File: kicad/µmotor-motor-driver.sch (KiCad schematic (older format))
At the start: 7 parts, among them J501 1, J502 2, U501 DRV8870, U502 INA180A1

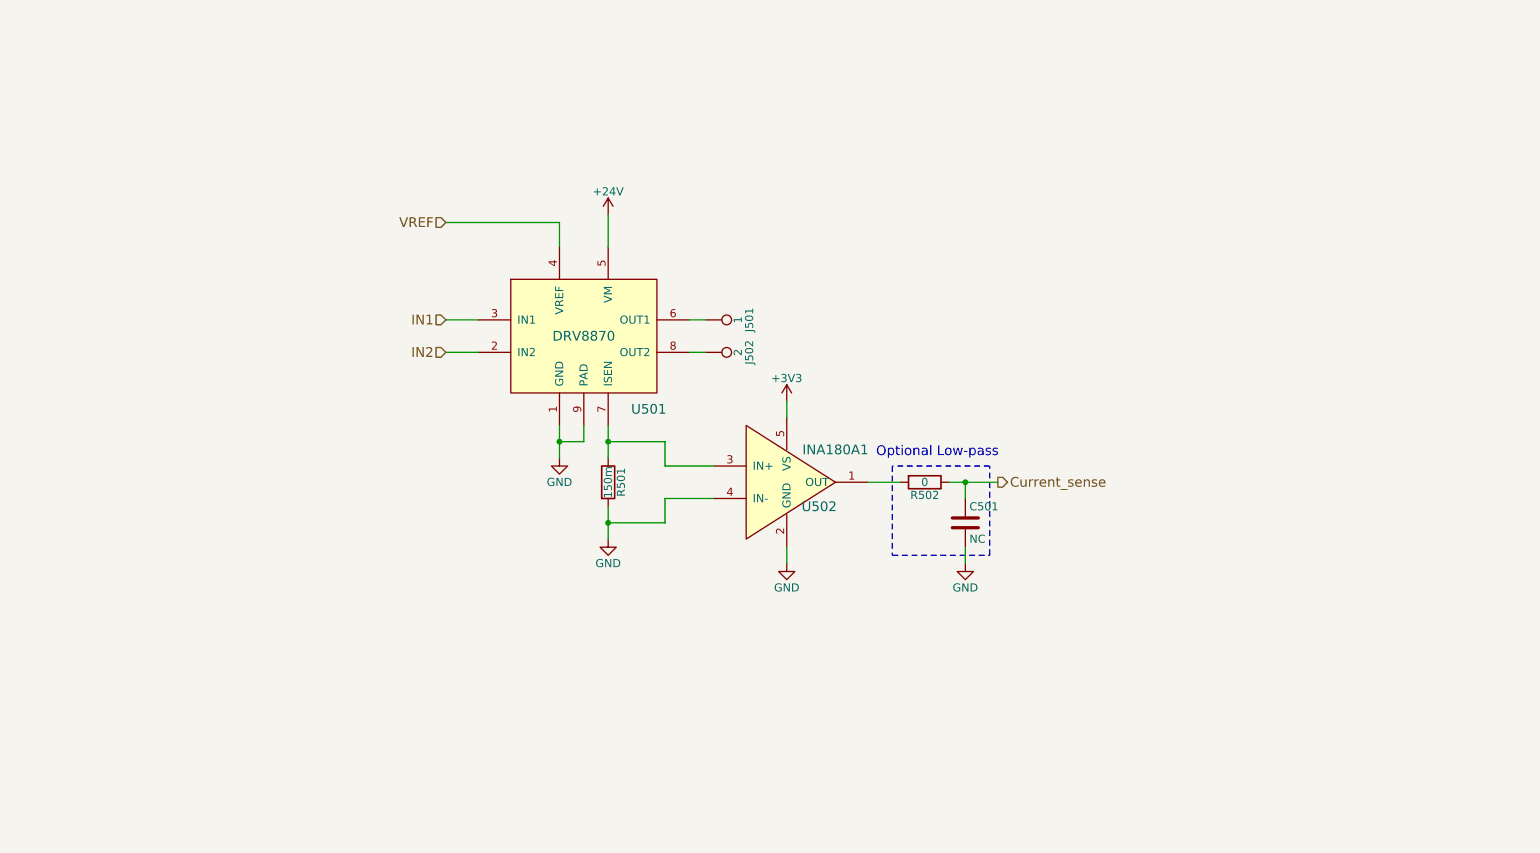
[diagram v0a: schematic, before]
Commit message: second design: STM32L432KC µC with DRV8323S gate driver and FDMD82xx FETs
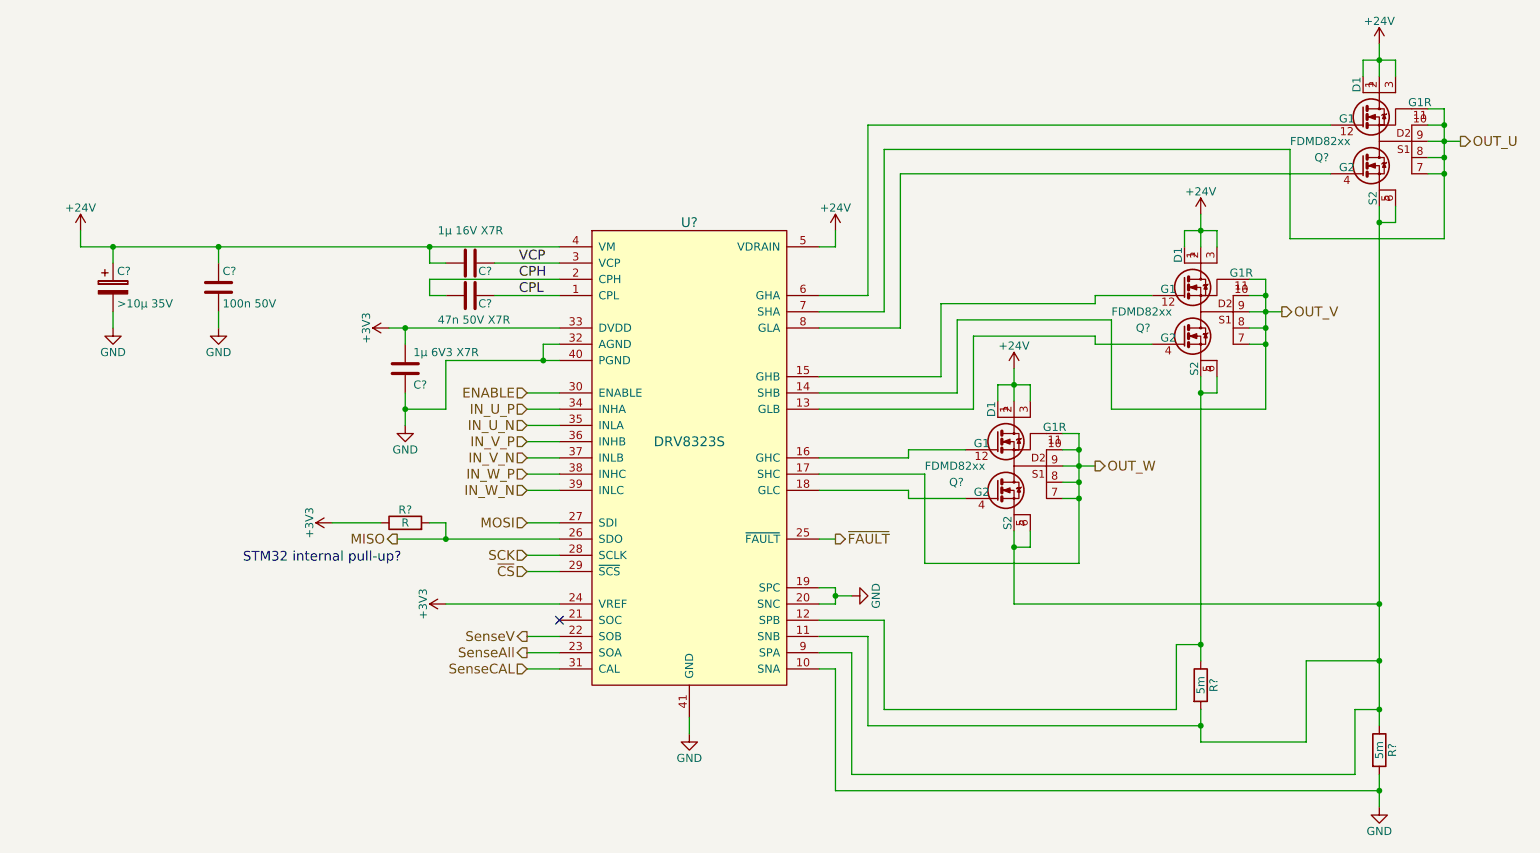
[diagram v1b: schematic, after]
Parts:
- removed C501: NC, Capacitors_SMD:C_0603, symbol C
- removed J501: 1, Measurement_Points:Measurement_Point_Round-SMD-Pad_Small, symbol TEST_1P
- removed J502: 2, Measurement_Points:Measurement_Point_Round-SMD-Pad_Small, symbol TEST_1P
- removed R501: 150m, Resistors_SMD:R_0805, symbol R
- removed R502: 0, Resistors_SMD:R_0603, symbol R
- removed U501: DRV8870, HSOP-8:HSOP-8, symbol DRV8870
- removed U502: INA180A1, TO_SOT_Packages_SMD:SOT-23-5, symbol INA180A
- added C?: 1µ 16V X7R, symbol C
- added C?: 47n 50V X7R, symbol C
- added C?: 100n 50V, symbol C
- added C?: >10µ 35V, symbol CP
- added C?: 1µ 6V3 X7R, symbol C
- added Q? (x3): FDMD82xx, symbol FDMD82xx
- added R?: R, symbol R
- added R? (x2): 5m, symbol R
- added U?: DRV8323S, symbol DRV8323S
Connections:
- net +24V: now also C?.1, C?.1, C?.2, Q?.1 (D1), Q?.1 (D1), Q?.1 (D1), Q?.13 (D1), Q?.13 (D1), Q?.13 (D1), Q?.2, Q?.2, Q?.2, Q?.3, Q?.3, Q?.3, U?.4 (VM), U?.5 (VDRAIN)
- net +3V3: now also C?.1, R?.1, U?.24 (VREF), U?.33 (DVDD)
- net GND: now also C?.2, C?.2, C?.2, R?.2, U?.10 (SNA), U?.19 (SPC), U?.20 (SNC), U?.32 (AGND), U?.40 (PGND), U?.41 (GND)
- new net: Q?.14 (S2), Q?.14 (S2), Q?.5 (S2), Q?.5 (S2), Q?.6, Q?.6, R?.1, R?.2, U?.11 (SNB), U?.9 (SPA)
- new net: Q?.14 (S2), Q?.5 (S2), Q?.6, R?.1, U?.12 (SPB)
- new net: Q?.4 (G2), U?.13 (GLB)
- new net: Q?.12 (G1), U?.15 (GHB)
- new net: Q?.12 (G1), U?.16 (GHC)
- new net: Q?.4 (G2), U?.18 (GLC)
- new net: Q?.12 (G1), U?.6 (GHA)
- new net: Q?.4 (G2), U?.8 (GLA)
- new net CPH: C?.2, U?.2 (CPH)
- new net CPL: C?.1, U?.1 (CPL)
- new net ENABLE: U?.30 (ENABLE)
- new net IN_U_N: U?.35 (INLA)
- new net IN_U_P: U?.34 (INHA)
- new net IN_V_N: U?.37 (INLB)
- new net IN_V_P: U?.36 (INHB)
- new net IN_W_N: U?.39 (INLC)
- new net IN_W_P: U?.38 (INHC)
- new net MISO: R?.2, U?.26 (SDO)
- new net MOSI: U?.27 (SDI)
- new net OUT_U: Q?.10, Q?.11 (G1R), Q?.7, Q?.8, Q?.9, U?.7 (SHA)
- new net OUT_V: Q?.10, Q?.11 (G1R), Q?.7, Q?.8, Q?.9, U?.14 (SHB)
- new net OUT_W: Q?.10, Q?.11 (G1R), Q?.7, Q?.8, Q?.9, U?.17 (SHC)
- new net SCK: U?.28 (SCLK)
- new net SenseAll: U?.23 (SOA)
- new net SenseCAL: U?.31 (CAL)
- new net SenseV: U?.22 (SOB)
- new net VCP: C?.1, U?.3 (VCP)
- new net ~CS: U?.29 (~SCS)
- new net ~FAULT: U?.25 (~FAULT)
- no-connect marks 0 -> 1
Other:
- note added: "STM32 internal pull-up?"
- note removed: "Optional Low-pass"

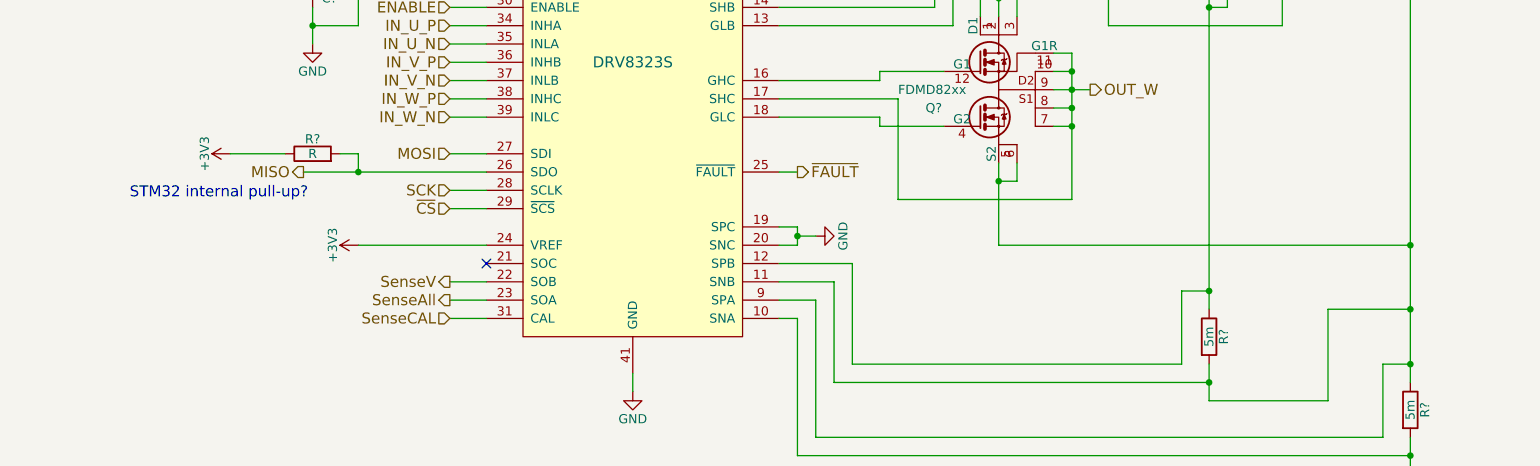
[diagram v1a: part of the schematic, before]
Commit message: update µC pinout, motor driver, CubeMX, add 3V3 regulator and temperature sensor
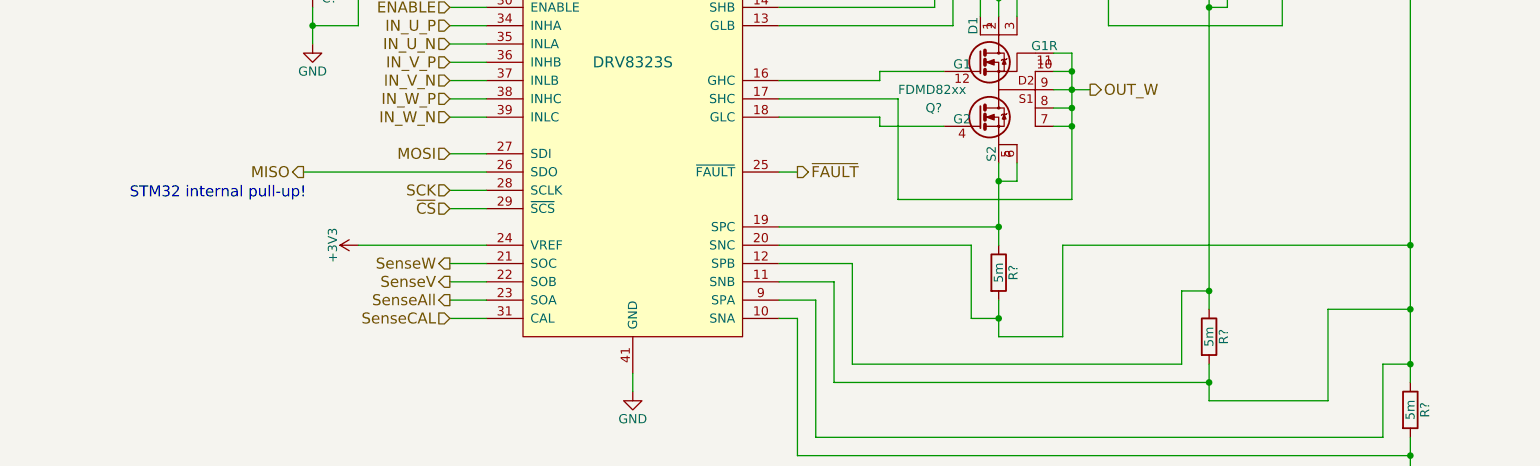
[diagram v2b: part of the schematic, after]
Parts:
- removed R?: R, symbol R
- added R?: 5m, symbol R
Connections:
- net GND: no longer U?.19 (SPC), U?.20 (SNC)
- net at Q?.14 (S2), Q?.5 (S2), Q?.6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: now also U?.20 (SNC), R?.2; no longer Q?.14 (S2), Q?.5 (S2), Q?.6
- net SenseW: now reaches U?.21 (SOC)
- new net: Q?.14 (S2), Q?.5 (S2), Q?.6, R?.1, U?.19 (SPC)
- no-connect marks 1 -> 0
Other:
- note added: "STM32 internal pull-up!"
- note removed: "STM32 internal pull-up?"
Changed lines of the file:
@@
 LIBS:drv8323s
 LIBS:FDMD82xx
+LIBS:ncp4623
+LIBS:TMP006
 LIBS:µmotor-cache
 EELAYER 25 0
@@
 $Descr A4 11693 8268
 encoding utf-8
-Sheet 4 6
+Sheet 3 6
 Title "µmotor - Micro Motor Controller"
 Date "2017-09-14"
@@
 Text HLabel 4850 4900 0    60   Input ~ 0
 ~CS
-$Comp
-L R R?
-U 1 1 5A4FECE8
-P 4100 4600
-F 0 "R?" V 4180 4600 50  0000 C CNN
-F 1 "R" V 4100 4600 50  0000 C CNN
-F 2 "" V 4030 4600 50  0001 C CNN
-F 3 "" H 4100 4600 50  0001 C CNN
-	1    4100 4600
-	0    -1   -1   0
-$EndComp
-$Comp
-L +3V3 #PWR?
-U 1 1 5A4FEE5D
-P 3650 4600
-F 0 "#PWR?" H 3650 4450 50  0001 C CNN
-F 1 "+3V3" H 3650 4740 50  0000 C CNN
-F 2 "" H 3650 4600 50  0001 C CNN
-F 3 "" H 3650 4600 50  0001 C CNN
-	1    3650 4600
-	0    -1   -1   0
-$EndComp
 Text Notes 3100 4850 0    60   ~ 0
-STM32 internal pull-up?
+STM32 internal pull-up!
 $Comp
 L GND #PWR?
@@
 	4850 5500 5050 5500
 Wire Wire Line
-	4250 4600 4350 4600
-Wire Wire Line
-	4350 4600 4350 4700
-Wire Wire Line
 	4050 4700 5050 4700
-Connection ~ 4350 4700
 Wire Wire Line
 	4850 4600 5050 4600
@@
 Wire Wire Line
 	4850 4900 5050 4900
-Wire Wire Line
-	3650 4600 3950 4600
 Wire Wire Line
 	5850 5900 5850 5800
@@
 	6850 5400 6650 5400
 Connection ~ 10100 5750
-Wire Wire Line
-	7850 5100 10100 5100
 Connection ~ 10100 5100
 Wire Wire Line
@@
 	7850 4650 7850 5100
 Connection ~ 7850 4750
-NoConn ~ 5050 5200
-$Comp
-L GND #PWR?
-U 1 1 5A523579
-P 6850 5050
-F 0 "#PWR?" H 6850 4800 50  0001 C CNN
-F 1 "GND" H 6850 4900 50  0000 C CNN
-F 2 "" H 6850 5050 50  0001 C CNN
-F 3 "" H 6850 5050 50  0001 C CNN
-	1    6850 5050
-	0    -1   -1   0
-$EndComp
-Wire Wire Line
-	6850 5050 6750 5050
-Wire Wire Line
-	6750 5000 6750 5100
-Wire Wire Line
-	6750 5000 6650 5000
-Wire Wire Line
-	6750 5100 6650 5100
-Connection ~ 6750 5050
+Text HLabel 4850 5200 0    60   Output ~ 0
+SenseW
+$Comp
+L R R?
+U 1 1 5A534BFF
+P 7850 5250
+F 0 "R?" V 7930 5250 50  0000 C CNN
+F 1 "5m" V 7850 5250 50  0000 C CNN
+F 2 "" V 7780 5250 50  0001 C CNN
+F 3 "" H 7850 5250 50  0001 C CNN
+	1    7850 5250
+	1    0    0    -1
+$EndComp
+Wire Wire Line
+	7850 5400 7850 5600
+Wire Wire Line
+	7850 5600 8200 5600
+Wire Wire Line
+	8200 5600 8200 5100
+Wire Wire Line
+	8200 5100 10100 5100
+Wire Wire Line
+	6650 5000 7850 5000
+Connection ~ 7850 5000
+Wire Wire Line
+	6650 5100 7700 5100
+Wire Wire Line
+	7700 5100 7700 5500
+Wire Wire Line
+	7700 5500 7850 5500
+Connection ~ 7850 5500
+Wire Wire Line
+	5050 5200 4850 5200
 $EndSCHEMATC

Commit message: layout: components placed
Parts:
- C301: renamed from C?; footprint (none) -> Capacitors_THT:CP_Radial_D4.0mm_P2.00mm
- C302, C303, C304, C305: renamed from C?; footprint (none) -> Capacitors_SMD:C_0603
- Q301, Q302, Q303: renamed from Q?; footprint (none) -> DFN-12-2EP_3.3x5mm_Pitch0.65mm:DFN-12-2EP_3.3x5mm_Pitch0.65mm
- R301, R302, R303: renamed from R?; footprint (none) -> Resistors_SMD:R_0603
- U301: renamed from U?; footprint (none) -> Housings_DFN_QFN:QFN-40-1EP_6x6mm_Pitch0.5mm
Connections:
- net +3V3: no longer C303.1, U301.33 (DVDD)
- new net 3V3_DRV: C303.1, U301.33 (DVDD)
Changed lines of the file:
@@
 LIBS:conn
 LIBS:linear
-LIBS:regul
-LIBS:74xx
-LIBS:cmos4000
-LIBS:adc-dac
-LIBS:memory
-LIBS:xilinx
-LIBS:microcontrollers
-LIBS:dsp
-LIBS:microchip
-LIBS:analog_switches
-LIBS:motorola
 LIBS:texas
-LIBS:intel
-LIBS:audio
 LIBS:interface
-LIBS:digital-audio
-LIBS:philips
-LIBS:display
-LIBS:cypress
-LIBS:siliconi
-LIBS:opto
-LIBS:atmel
 LIBS:contrib
 LIBS:valves
-LIBS:stm32
 LIBS:DRV8870
 LIBS:INA180A
@@
 LIBS:ncp4623
 LIBS:TMP006
+LIBS:stm32
 LIBS:µmotor-cache
 EELAYER 25 0
@@
 $EndDescr
 $Comp
-L +24V #PWR021
+L +24V #PWR012
 U 1 1 59BA7201
 P 2100 2800
-F 0 "#PWR021" H 2100 2650 50  0001 C CNN
+F 0 "#PWR012" H 2100 2650 50  0001 C CNN
 F 1 "+24V" H 2100 2940 50  0000 C CNN
 F 2 "" H 2100 2800 50  0001 C CNN
@@
 SenseCAL
 $Comp
-L DRV8323S U?
+L DRV8323S U301
 U 1 1 5A4FE001
 P 5850 4100
-F 0 "U?" H 5850 5450 60  0000 C CNN
+F 0 "U301" H 5850 5450 60  0000 C CNN
 F 1 "DRV8323S" H 5850 4100 60  0000 C CNN
-F 2 "" H 5850 4100 60  0001 C CNN
+F 2 "Housings_DFN_QFN:QFN-40-1EP_6x6mm_Pitch0.5mm" H 5850 4100 60  0001 C CNN
 F 3 "" H 5850 4100 60  0001 C CNN
 	1    5850 4100
@@
 ENABLE
 $Comp
-L C C?
+L C C304
 U 1 1 5A4FE181
 P 4500 3000
-F 0 "C?" V 4550 3050 50  0000 L CNN
+F 0 "C304" V 4550 3050 50  0000 L CNN
 F 1 "1µ 16V X7R" V 4300 2800 50  0000 L CNN
-F 2 "" H 4538 2850 50  0001 C CNN
+F 2 "Capacitors_SMD:C_0603" H 4538 2850 50  0001 C CNN
 F 3 "" H 4500 3000 50  0001 C CNN
 	1    4500 3000
@@
 VCP
 $Comp
-L C C?
+L C C305
 U 1 1 5A4FE29C
 P 4500 3200
-F 0 "C?" V 4550 3250 50  0000 L CNN
+F 0 "C305" V 4550 3250 50  0000 L CNN
 F 1 "47n 50V X7R" V 4650 3000 50  0000 L CNN
-F 2 "" H 4538 3050 50  0001 C CNN
+F 2 "Capacitors_SMD:C_0603" H 4538 3050 50  0001 C CNN
 F 3 "" H 4500 3200 50  0001 C CNN
 	1    4500 3200
@@
 CPL
 $Comp
-L C C?
+L C C302
 U 1 1 5A4FE3E8
 P 2950 3150
-F 0 "C?" H 2975 3250 50  0000 L CNN
+F 0 "C302" H 2975 3250 50  0000 L CNN
 F 1 "100n 50V" H 2975 3050 50  0000 L CNN
-F 2 "" H 2988 3000 50  0001 C CNN
+F 2 "Capacitors_SMD:C_0603" H 2988 3000 50  0001 C CNN
 F 3 "" H 2950 3150 50  0001 C CNN
 	1    2950 3150
@@
 $EndComp
 $Comp
-L CP C?
+L CP C301
 U 1 1 5A4FE464
 P 2300 3150
-F 0 "C?" H 2325 3250 50  0000 L CNN
+F 0 "C301" H 2325 3250 50  0000 L CNN
 F 1 ">10µ 35V" H 2325 3050 50  0000 L CNN
-F 2 "" H 2338 3000 50  0001 C CNN
+F 2 "Capacitors_THT:CP_Radial_D4.0mm_P2.00mm" H 2338 3000 50  0001 C CNN
 F 3 "" H 2300 3150 50  0001 C CNN
 	1    2300 3150
@@
 $EndComp
 $Comp
-L GND #PWR?
+L GND #PWR013
 U 1 1 5A4FE4D1
 P 2300 3400
-F 0 "#PWR?" H 2300 3150 50  0001 C CNN
+F 0 "#PWR013" H 2300 3150 50  0001 C CNN
 F 1 "GND" H 2300 3250 50  0000 C CNN
 F 2 "" H 2300 3400 50  0001 C CNN
@@
 $EndComp
 $Comp
-L GND #PWR?
+L GND #PWR014
 U 1 1 5A4FE4F8
 P 2950 3400
-F 0 "#PWR?" H 2950 3150 50  0001 C CNN
+F 0 "#PWR014" H 2950 3150 50  0001 C CNN
 F 1 "GND" H 2950 3250 50  0000 C CNN
 F 2 "" H 2950 3400 50  0001 C CNN
@@
 $EndComp
 $Comp
-L C C?
+L C C303
 U 1 1 5A4FE71A
 P 4100 3650
-F 0 "C?" H 4150 3550 50  0000 L CNN
+F 0 "C303" H 4150 3550 50  0000 L CNN
 F 1 "1µ 6V3 X7R" H 4150 3750 50  0000 L CNN
-F 2 "" H 4138 3500 50  0001 C CNN
+F 2 "Capacitors_SMD:C_0603" H 4138 3500 50  0001 C CNN
 F 3 "" H 4100 3650 50  0001 C CNN
 	1    4100 3650
@@
 $EndComp
 $Comp
-L +3V3 #PWR?
-U 1 1 5A4FE7D3
-P 4000 3400
-F 0 "#PWR?" H 4000 3250 50  0001 C CNN
-F 1 "+3V3" H 4000 3540 50  0000 C CNN
-F 2 "" H 4000 3400 50  0001 C CNN
-F 3 "" H 4000 3400 50  0001 C CNN
-	1    4000 3400
-	0    -1   -1   0
-$EndComp
-$Comp
-L GND #PWR?
+L GND #PWR015
 U 1 1 5A4FE87C
 P 4100 4000
-F 0 "#PWR?" H 4100 3750 50  0001 C CNN
+F 0 "#PWR015" H 4100 3750 50  0001 C CNN
 F 1 "GND" H 4100 3850 50  0000 C CNN
 F 2 "" H 4100 4000 50  0001 C CNN
@@
 STM32 internal pull-up!
 $Comp
-L GND #PWR?
+L GND #PWR016
 U 1 1 5A4FF46D
 P 5850 5900
-F 0 "#PWR?" H 5850 5650 50  0001 C CNN
+F 0 "#PWR016" H 5850 5650 50  0001 C CNN
 F 1 "GND" H 5850 5750 50  0000 C CNN
 F 2 "" H 5850 5900 50  0001 C CNN
@@
 $EndComp
 $Comp
-L FDMD82xx Q?
+L FDMD82xx Q303
 U 1 1 5A50285C
 P 10050 2250
-F 0 "Q?" H 9700 2150 50  0000 L CNN
+F 0 "Q303" H 9700 2150 50  0000 L CNN
 F 1 "FDMD82xx" H 9550 2250 50  0000 L CNN
-F 2 "" H 10150 2300 60  0001 C CNN
+F 2 "DFN-12-2EP_3.3x5mm_Pitch0.65mm:DFN-12-2EP_3.3x5mm_Pitch0.65mm" H 10150 2300 60  0001 C CNN
 F 3 "" H 10000 2400 50  0001 L CNN
 	1    10050 2250
@@
 $EndComp
 $Comp
-L +24V #PWR?
+L +24V #PWR017
 U 1 1 5A502CAF
 P 10100 1650
-F 0 "#PWR?" H 10100 1500 50  0001 C CNN
+F 0 "#PWR017" H 10100 1500 50  0001 C CNN
 F 1 "+24V" H 10100 1790 50  0000 C CNN
 F 2 "" H 10100 1650 50  0001 C CNN
@@
 $EndComp
 $Comp
-L +24V #PWR?
+L +24V #PWR018
 U 1 1 5A5036BC
 P 6750 2800
-F 0 "#PWR?" H 6750 2650 50  0001 C CNN
+F 0 "#PWR018" H 6750 2650 50  0001 C CNN
 F 1 "+24V" H 6750 2940 50  0000 C CNN
 F 2 "" H 6750 2800 50  0001 C CNN
@@
 OUT_U
 $Comp
-L FDMD82xx Q?
+L FDMD82xx Q301
 U 1 1 5A505C4C
 P 7800 4250
-F 0 "Q?" H 7450 4150 50  0000 L CNN
+F 0 "Q301" H 7450 4150 50  0000 L CNN
 F 1 "FDMD82xx" H 7300 4250 50  0000 L CNN
-F 2 "" H 7900 4300 60  0001 C CNN
+F 2 "DFN-12-2EP_3.3x5mm_Pitch0.65mm:DFN-12-2EP_3.3x5mm_Pitch0.65mm" H 7900 4300 60  0001 C CNN
 F 3 "" H 7750 4400 50  0001 L CNN
 	1    7800 4250
@@
 $EndComp
 $Comp
-L +24V #PWR?
+L +24V #PWR019
 U 1 1 5A505C52
 P 7850 3650
-F 0 "#PWR?" H 7850 3500 50  0001 C CNN
+F 0 "#PWR019" H 7850 3500 50  0001 C CNN
 F 1 "+24V" H 7850 3790 50  0000 C CNN
 F 2 "" H 7850 3650 50  0001 C CNN
@@
 OUT_W
 $Comp
-L FDMD82xx Q?
+L FDMD82xx Q302
 U 1 1 5A506004
 P 8950 3300
-F 0 "Q?" H 8600 3200 50  0000 L CNN
+F 0 "Q302" H 8600 3200 50  0000 L CNN
 F 1 "FDMD82xx" H 8450 3300 50  0000 L CNN
-F 2 "" H 9050 3350 60  0001 C CNN
+F 2 "DFN-12-2EP_3.3x5mm_Pitch0.65mm:DFN-12-2EP_3.3x5mm_Pitch0.65mm" H 9050 3350 60  0001 C CNN
 F 3 "" H 8900 3450 50  0001 L CNN
 	1    8950 3300
@@
 $EndComp
 $Comp
-L +24V #PWR?
+L +24V #PWR020
 U 1 1 5A50600A
 P 9000 2700
-F 0 "#PWR?" H 9000 2550 50  0001 C CNN
+F 0 "#PWR020" H 9000 2550 50  0001 C CNN
 F 1 "+24V" H 9000 2840 50  0000 C CNN
 F 2 "" H 9000 2700 50  0001 C CNN
@@
 ~FAULT
 $Comp
-L R R?
+L R R302
 U 1 1 5A5066D4
 P 9000 5600
-F 0 "R?" V 9080 5600 50  0000 C CNN
+F 0 "R302" V 9080 5600 50  0000 C CNN
 F 1 "5m" V 9000 5600 50  0000 C CNN
-F 2 "" V 8930 5600 50  0001 C CNN
+F 2 "Resistors_SMD:R_0603" V 8930 5600 50  0001 C CNN
 F 3 "" H 9000 5600 50  0001 C CNN
 	1    9000 5600
@@
 $EndComp
 $Comp
-L R R?
+L R R303
 U 1 1 5A50692C
 P 10100 6000
-F 0 "R?" V 10180 6000 50  0000 C CNN
+F 0 "R303" V 10180 6000 50  0000 C CNN
 F 1 "5m" V 10100 6000 50  0000 C CNN
-F 2 "" V 10030 6000 50  0001 C CNN
+F 2 "Resistors_SMD:R_0603" V 10030 6000 50  0001 C CNN
 F 3 "" H 10100 6000 50  0001 C CNN
 	1    10100 6000
@@
 	4850 4400 5050 4400
 Wire Wire Line
-	4000 3400 5050 3400
-Wire Wire Line
 	4100 3400 4100 3500
-Connection ~ 4100 3400
 Wire Wire Line
 	4100 3800 4100 4000
@@
 	6750 4700 6650 4700
 $Comp
-L GND #PWR?
+L GND #PWR021
 U 1 1 5A507920
 P 10100 6350
-F 0 "#PWR?" H 10100 6100 50  0001 C CNN
+F 0 "#PWR021" H 10100 6100 50  0001 C CNN
 F 1 "GND" H 10100 6200 50  0000 C CNN
 F 2 "" H 10100 6350 50  0001 C CNN
@@
 Connection ~ 10100 5450
 $Comp
-L +3V3 #PWR?
+L +3V3 #PWR022
 U 1 1 5A521C1B
 P 4350 5100
-F 0 "#PWR?" H 4350 4950 50  0001 C CNN
+F 0 "#PWR022" H 4350 4950 50  0001 C CNN
 F 1 "+3V3" H 4350 5240 50  0000 C CNN
 F 2 "" H 4350 5100 50  0001 C CNN
@@
 SenseW
 $Comp
-L R R?
+L R R301
 U 1 1 5A534BFF
 P 7850 5250
-F 0 "R?" V 7930 5250 50  0000 C CNN
+F 0 "R301" V 7930 5250 50  0000 C CNN
 F 1 "5m" V 7850 5250 50  0000 C CNN
-F 2 "" V 7780 5250 50  0001 C CNN
+F 2 "Resistors_SMD:R_0603" V 7780 5250 50  0001 C CNN
 F 3 "" H 7850 5250 50  0001 C CNN
 	1    7850 5250
@@
 Wire Wire Line
 	5050 5200 4850 5200
+Wire Wire Line
+	3850 3400 5050 3400
+Text Label 3850 3400 0    60   ~ 0
+3V3_DRV
+Connection ~ 4100 3400
 $EndSCHEMATC
